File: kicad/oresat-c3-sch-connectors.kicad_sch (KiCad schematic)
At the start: 29 parts, among them J1 J-SAMTEC-TFM-120-01-L-D-RA, J2 J-TE-Debug-2-1734592-0, J3 J-MOLEX-SMPM-73300-003X, J4 J-MOLEX-SMPM-73300-003X

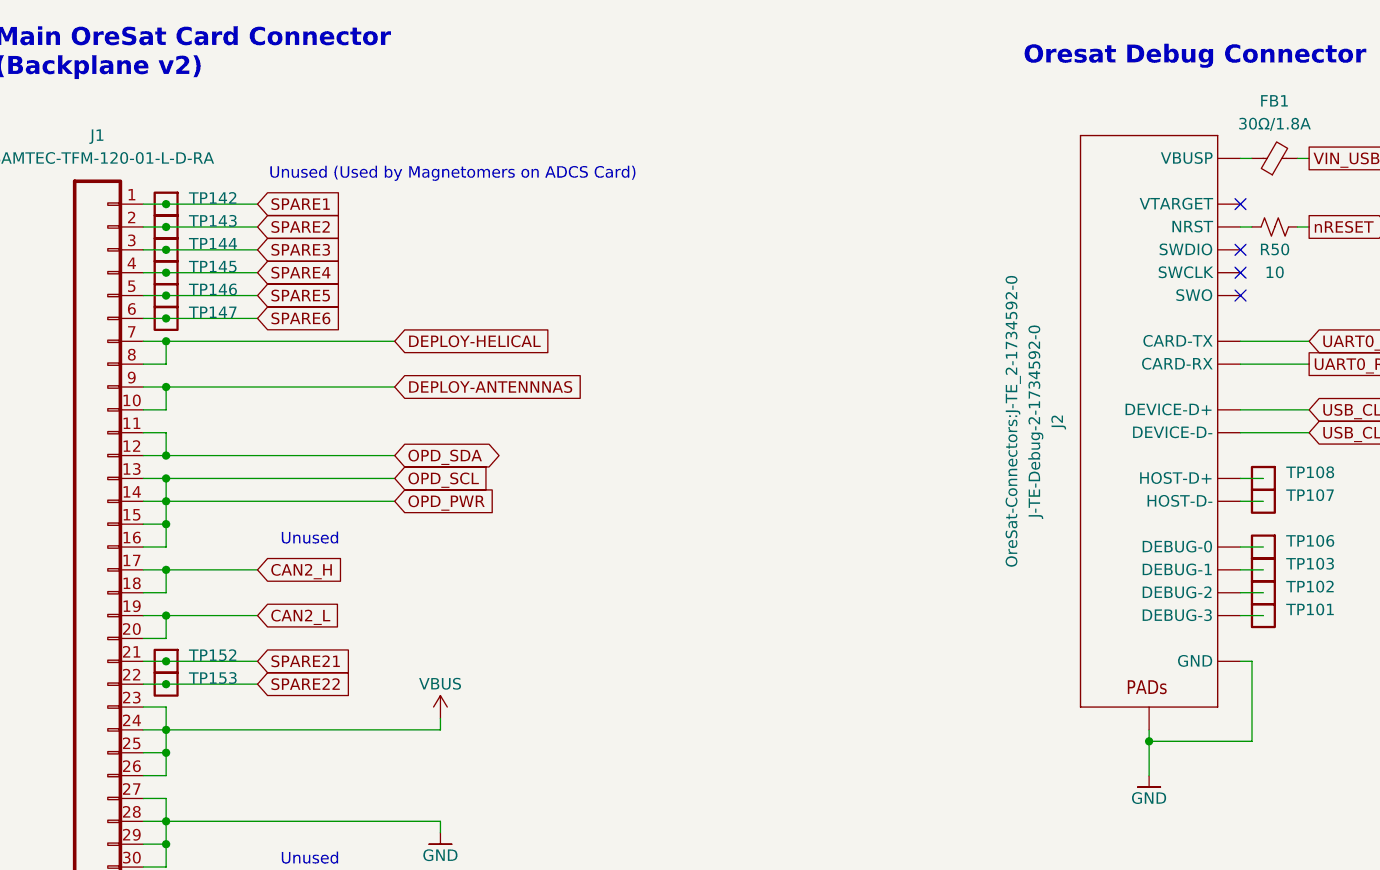
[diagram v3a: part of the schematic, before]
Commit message: First round of ERC fixes.
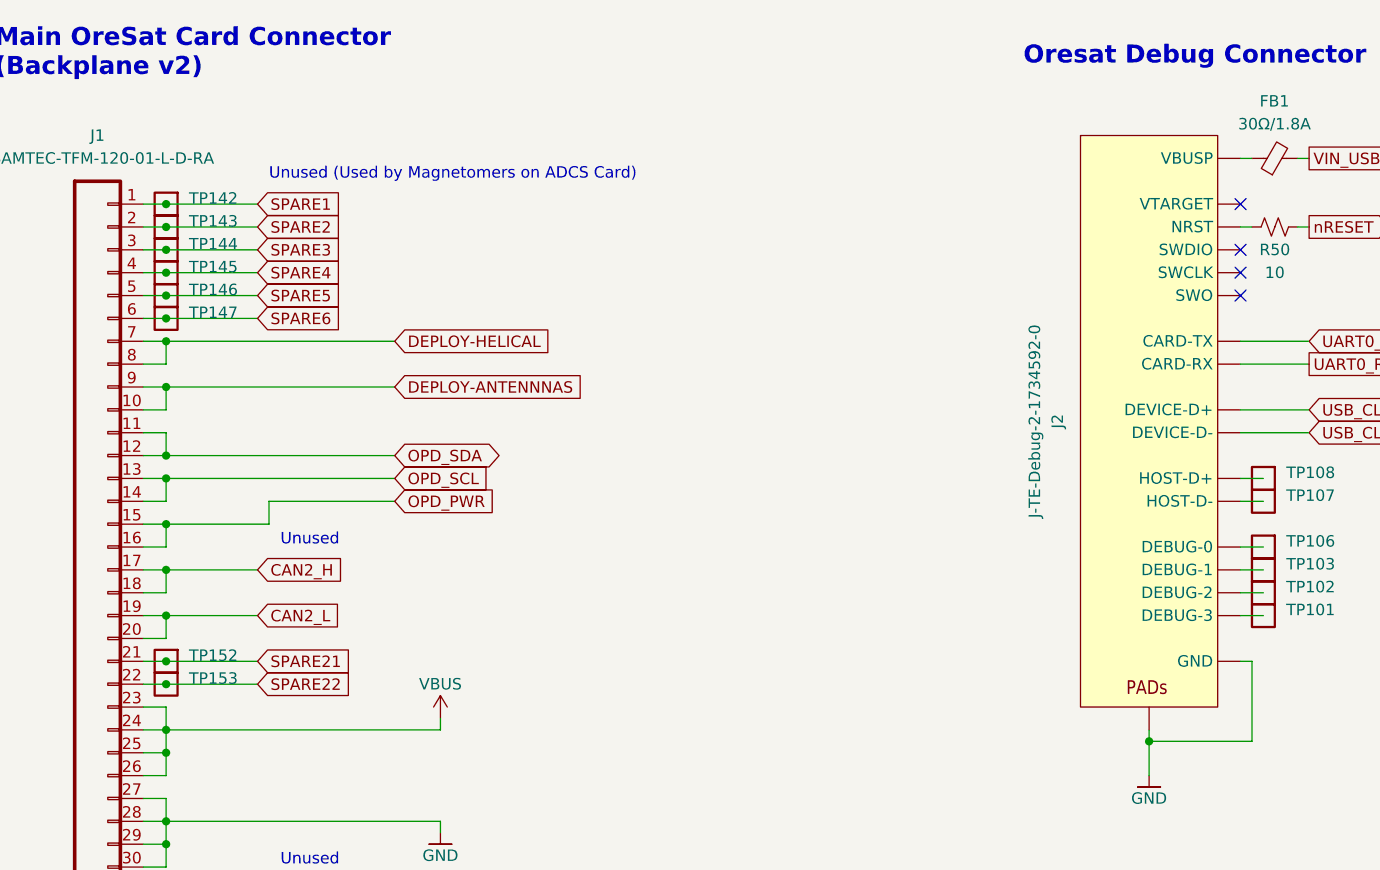
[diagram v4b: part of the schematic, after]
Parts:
- J1: footprint OreSat-Connectors:J-SAMTEC-TFM-120-X1-XXX-D-RA -> oresat-footprints:J-SAMTEC-TFM-120-X1-XXX-D-RA; symbol OreSat-Connectors:J-SAMTEC-TFM-120-01-L-D-RA -> oresat-connectors:J-SAMTEC-TFM-120-01-L-D-RA
- J2: footprint OreSat-Connectors:J-TE_2-1734592-0 -> oresat-footprints:J-TE_2-1734592-0; symbol OreSat-Connectors:J-TE-Debug-2-1734592-0 -> oresat-connectors:J-TE-Debug-2-1734592-0
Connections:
- net OPD_PWR: no longer J1.13, J1.14
- new net OPD_SCL: J1.13, J1.14
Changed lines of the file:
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@@
   (junction (at 200.66 140.97) (diameter 0) (color 0 0 0 0)
   )
-  (junction (at 91.44 114.3) (diameter 0) (color 0 0 0 0)
-  )
   (junction (at 91.44 109.22) (diameter 0) (color 0 0 0 0)
   )
   (junction (at 91.44 81.28) (diameter 0) (color 0 0 0 0)
   )
+  (junction (at 91.44 83.82) (diameter 0) (color 0 0 0 0)
+  )
+  (junction (at 91.44 127) (diameter 0) (color 0 0 0 0)
+  )
+  (junction (at 91.44 101.6) (diameter 0) (color 0 0 0 0)
+  )
+  (junction (at 91.44 93.98) (diameter 0) (color 0 0 0 0)
+  )
   (junction (at 91.44 116.84) (diameter 0) (color 0 0 0 0)
-  )
-  (junction (at 91.44 83.82) (diameter 0) (color 0 0 0 0)
-  )
-  (junction (at 91.44 127) (diameter 0) (color 0 0 0 0)
-  )
-  (junction (at 91.44 101.6) (diameter 0) (color 0 0 0 0)
-  )
-  (junction (at 91.44 93.98) (diameter 0) (color 0 0 0 0)
   )
   (junction (at 91.44 149.86) (diameter 0) (color 0 0 0 0)
@@
     (stroke (width 0) (type default))
   )
+  (wire (pts (xy 102.87 114.3) (xy 116.84 114.3))
+    (stroke (width 0) (type default))
+  )
   (wire (pts (xy 88.9 83.82) (xy 91.44 83.82))
     (stroke (width 0) (type default))
@@
     (stroke (width 0) (type default))
   )
-  (wire (pts (xy 91.44 116.84) (xy 91.44 114.3))
-    (stroke (width 0) (type default))
-  )
   (wire (pts (xy 196.85 176.53) (xy 201.93 176.53))
     (stroke (width 0) (type default))
@@
     (stroke (width 0) (type default))
   )
-  (wire (pts (xy 91.44 114.3) (xy 116.84 114.3))
-    (stroke (width 0) (type default))
-  )
   (wire (pts (xy 88.9 180.34) (xy 91.44 180.34))
     (stroke (width 0) (type default))
@@
     (stroke (width 0) (type default))
   )
+  (wire (pts (xy 102.87 116.84) (xy 102.87 114.3))
+    (stroke (width 0) (type default))
+  )
   (wire (pts (xy 91.44 177.8) (xy 116.84 177.8))
     (stroke (width 0) (type default))
@@
   )
   (wire (pts (xy 213.36 111.76) (xy 210.82 111.76))
+    (stroke (width 0) (type default))
+  )
+  (wire (pts (xy 91.44 116.84) (xy 102.87 116.84))
     (stroke (width 0) (type default))
   )
@@
     )
   )
-  (symbol (lib_id "OreSat-Connectors:J-TE-Debug-2-1734592-0") (at 200.66 104.14 0) (unit 1)
+  (symbol (lib_id "oresat-connectors:J-TE-Debug-2-1734592-0") (at 200.66 104.14 0) (unit 1)
     (in_bom yes) (on_board yes) (dnp no) (fields_autoplaced)
     (property "Reference" "J2" (at 190.5 105.41 90)
@@
       (effects (font (size 1.27 1.27)))
     )
-    (property "Footprint" "OreSat-Connectors:J-TE_2-1734592-0" (at 185.42 105.41 90)
-      (effects (font (size 1.27 1.27)))
+    (property "Footprint" "oresat-footprints:J-TE_2-1734592-0" (at 200.66 62.23 0)
+      (effects (font (size 1.27 1.27)) hide)
     )
     (property "Datasheet" "" (at 200.66 95.25 0)
@@
     )
   )
-  (symbol (lib_id "OreSat-Connectors:J-SAMTEC-TFM-120-01-L-D-RA") (at 83.82 129.54 0) (unit 1)
+  (symbol (lib_id "oresat-connectors:J-SAMTEC-TFM-120-01-L-D-RA") (at 83.82 129.54 0) (unit 1)
     (in_bom yes) (on_board yes) (dnp no) (fields_autoplaced)
     (property "Reference" "J1" (at 83.82 73.66 0)
@@
       (effects (font (size 1.27 1.27)))
     )
-    (property "Footprint" "OreSat-Connectors:J-SAMTEC-TFM-120-X1-XXX-D-RA" (at 83.82 129.54 0)
-      (effects (font (size 1.27 1.27)) hide)
-    )
+    (property "Footprint" "oresat-footprints:J-SAMTEC-TFM-120-X1-XXX-D-RA" (at 83.82 129.54 0)
+      (effects (font (size 1.27 1.27)) hide)
+    )
